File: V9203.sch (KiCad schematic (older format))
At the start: 62 parts, among them J1 RJ45, J4 Screw_Terminal_1x04, J6 CONN_01X06, J7 GS3, J8 GS3, U1 V9203, Y1 Crystal_GND24

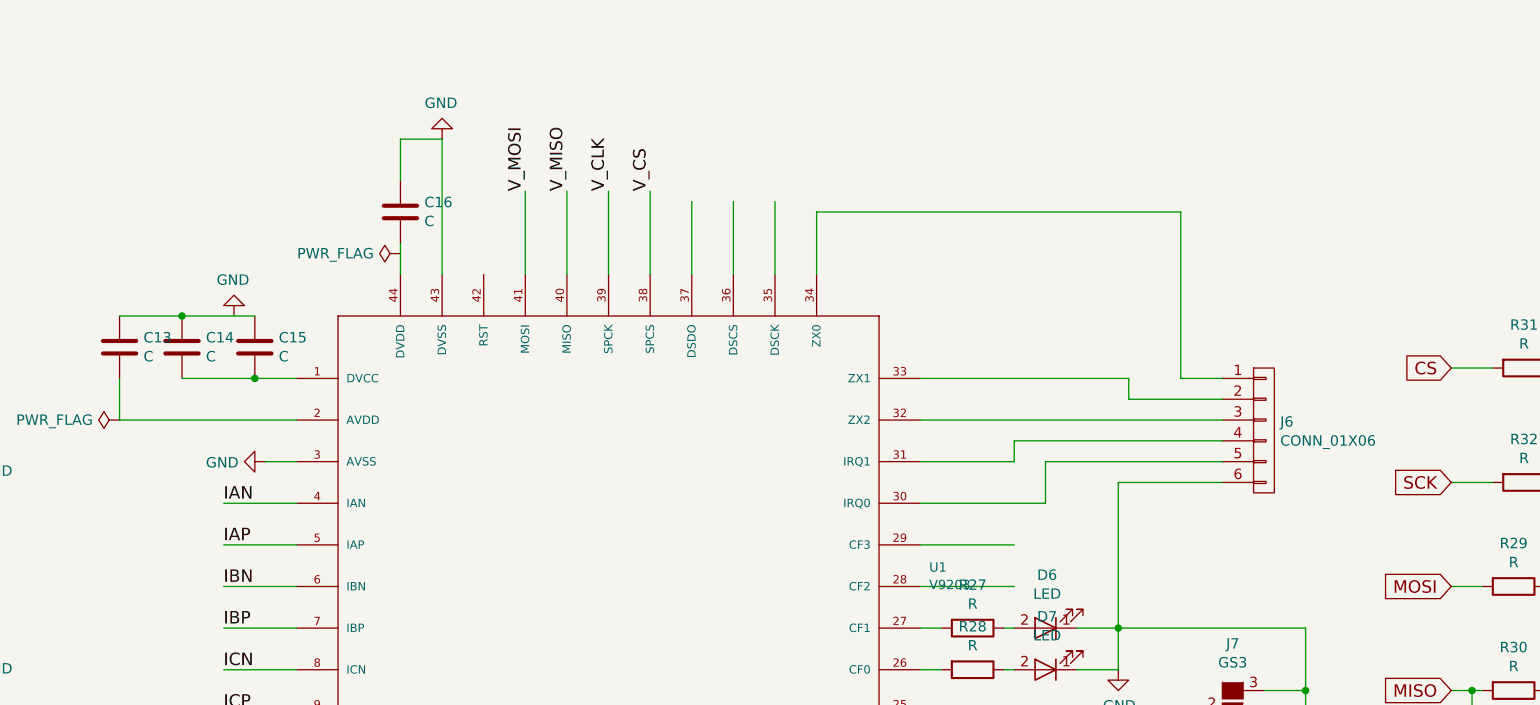
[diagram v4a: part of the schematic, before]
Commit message: Added more signals to JST connector including DMA
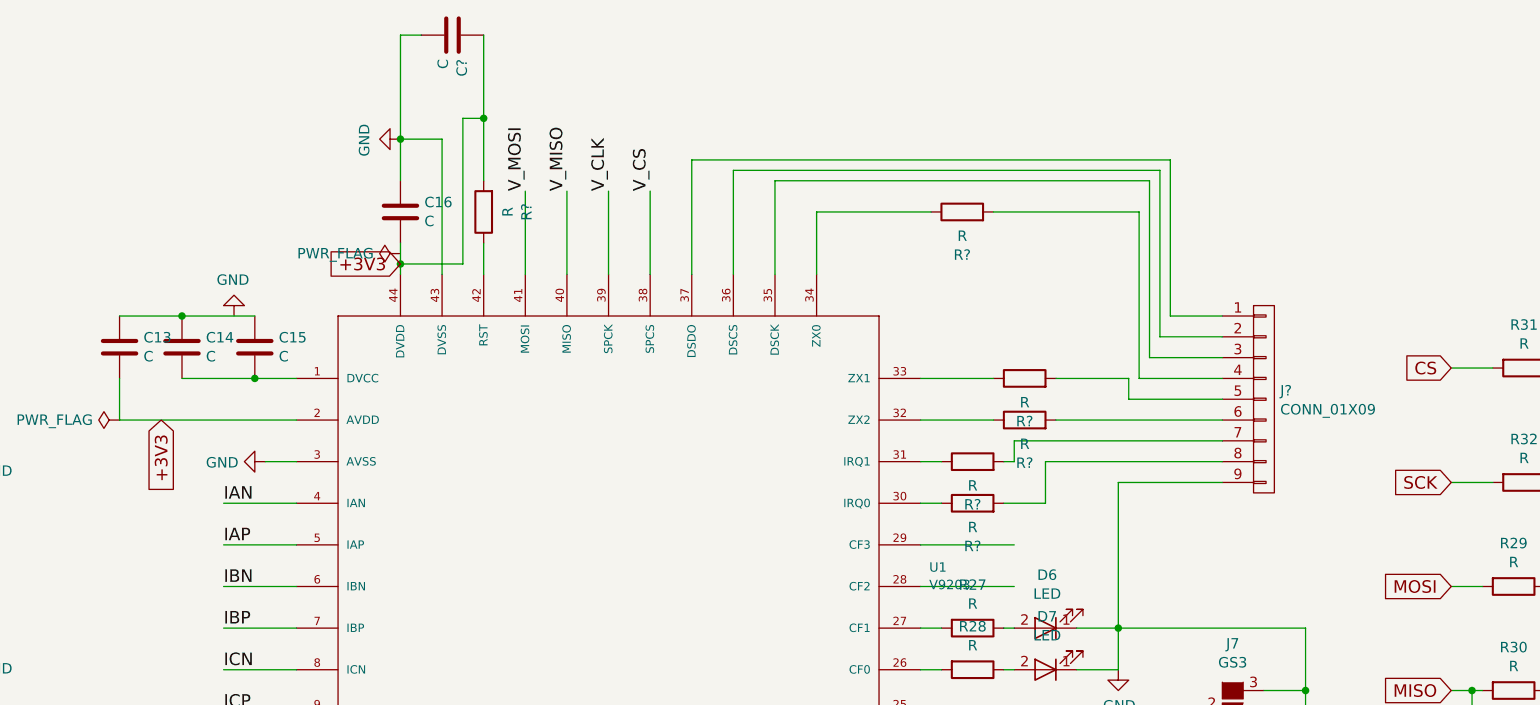
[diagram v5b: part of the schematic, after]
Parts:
- removed J6: CONN_01X06, Connectors_JST:JST_PH_B6B-PH-SM4-TB_06x2.00mm_Straight, symbol CONN_01X06
- added C?: C, Capacitors_SMD:C_0402, symbol C
- added J?: CONN_01X09, symbol CONN_01X09
- added R? (x6): R, Resistors_SMD:R_0402, symbol R
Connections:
- wire segments 167 -> 187

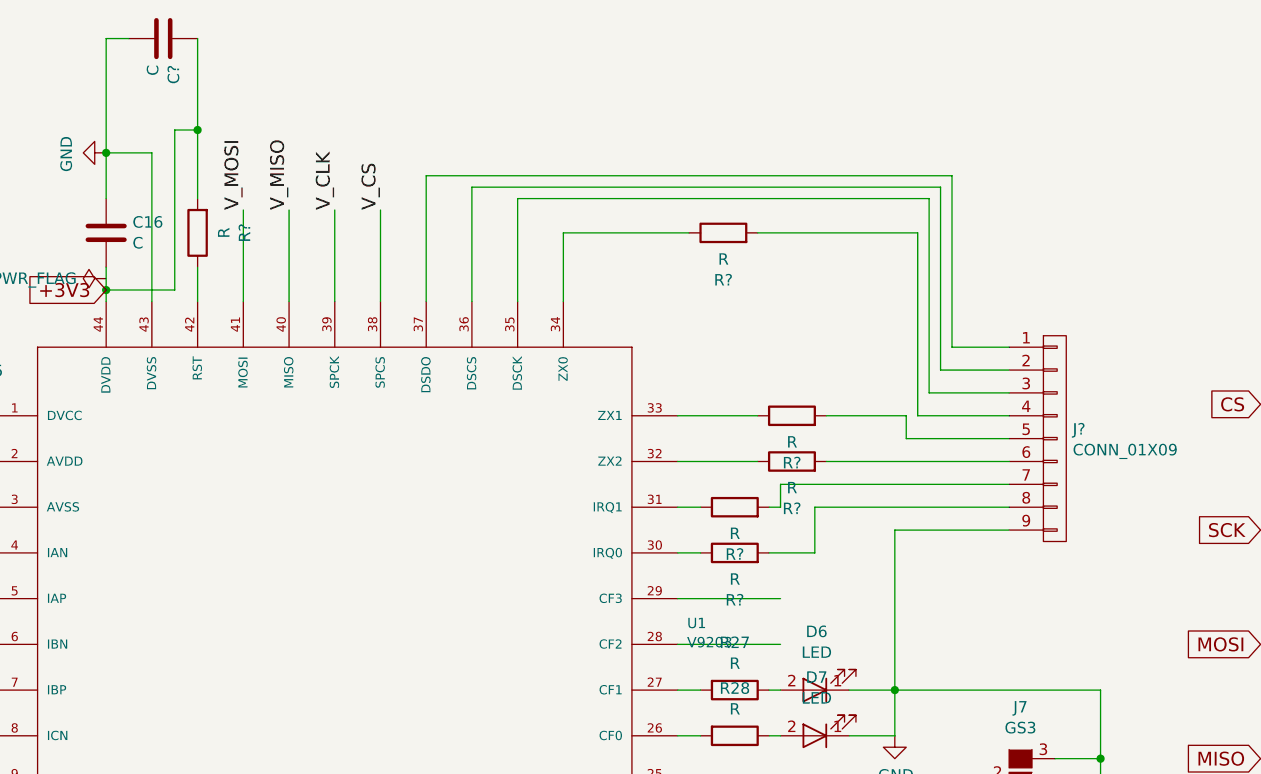
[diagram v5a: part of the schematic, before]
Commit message: Added more signals to JST connector including DMA
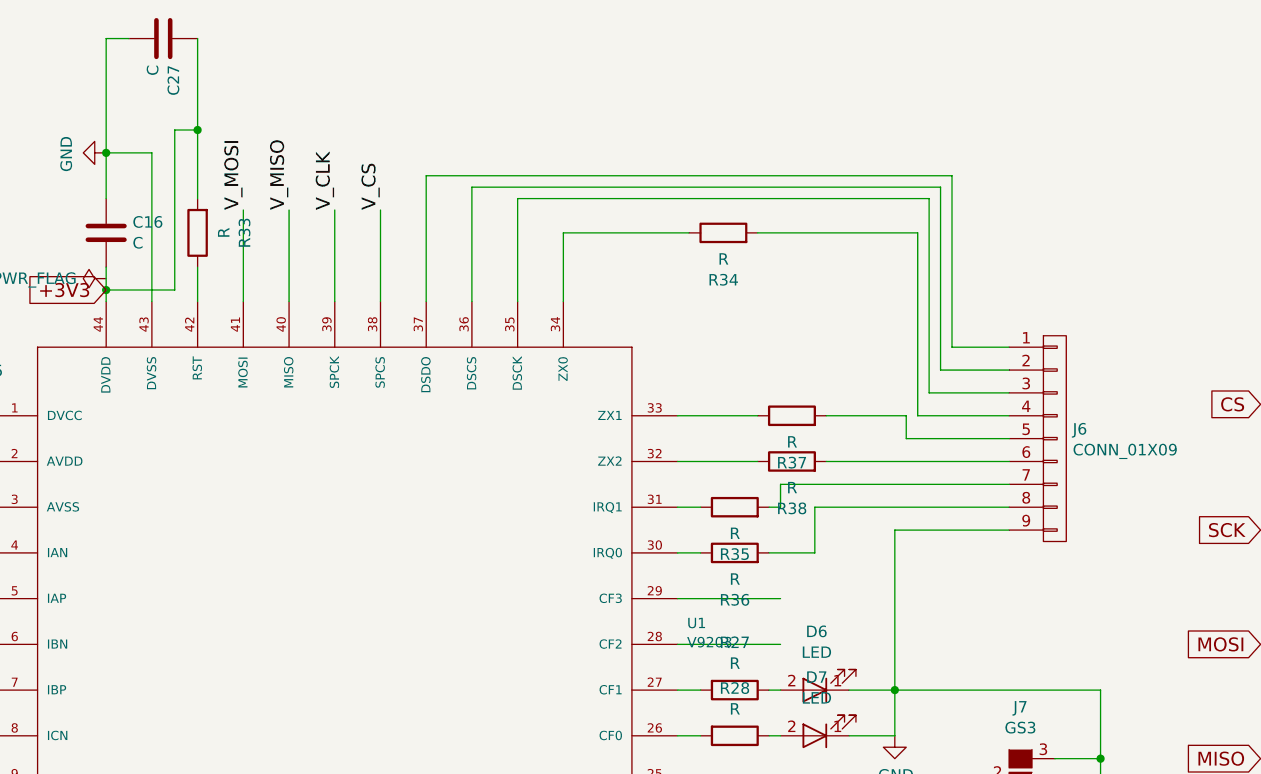
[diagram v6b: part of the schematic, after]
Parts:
- J6: renamed from J?; footprint (none) -> Connectors_JST:JST_SH_SM09B-SRSS-TB_09x1.00mm_Angled
- gave numbers to parts that had none: 7
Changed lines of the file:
@@
 +3V3
 $Comp
-L R R?
+L R R33
 U 1 1 5900142F
 P 5100 1700
-F 0 "R?" V 4893 1700 50  0000 C CNN
+F 0 "R33" V 4893 1700 50  0000 C CNN
 F 1 "R" V 4984 1700 50  0000 C CNN
 F 2 "Resistors_SMD:R_0402" V 2480 -450 50  0001 C CNN
@@
 $EndComp
 $Comp
-L C C?
+L C C27
 U 1 1 590019CE
 P 4950 850
-F 0 "C?" H 4835 804 50  0000 R CNN
+F 0 "C27" H 4835 804 50  0000 R CNN
 F 1 "C" H 4835 895 50  0000 R CNN
 F 2 "Capacitors_SMD:C_0402" H 3388 -2250 50  0001 C CNN
@@
 $EndComp
 $Comp
-L R R?
+L R R37
 U 1 1 590033EF
 P 7700 2500
-F 0 "R?" V 7493 2500 50  0000 C CNN
+F 0 "R37" V 7493 2500 50  0000 C CNN
 F 1 "R" V 7584 2500 50  0000 C CNN
 F 2 "Resistors_SMD:R_0402" V 5080 350 50  0001 C CNN
@@
 $EndComp
 $Comp
-L R R?
+L R R38
 U 1 1 59003D0A
 P 7700 2700
-F 0 "R?" V 7493 2700 50  0000 C CNN
+F 0 "R38" V 7493 2700 50  0000 C CNN
 F 1 "R" V 7584 2700 50  0000 C CNN
 F 2 "Resistors_SMD:R_0402" V 5080 550 50  0001 C CNN
@@
 $EndComp
 $Comp
-L R R?
+L R R35
 U 1 1 59003DA0
 P 7450 2900
-F 0 "R?" V 7243 2900 50  0000 C CNN
+F 0 "R35" V 7243 2900 50  0000 C CNN
 F 1 "R" V 7334 2900 50  0000 C CNN
 F 2 "Resistors_SMD:R_0402" V 4830 750 50  0001 C CNN
@@
 $EndComp
 $Comp
-L R R?
+L R R36
 U 1 1 59003E4E
 P 7450 3100
-F 0 "R?" V 7243 3100 50  0000 C CNN
+F 0 "R36" V 7243 3100 50  0000 C CNN
 F 1 "R" V 7334 3100 50  0000 C CNN
 F 2 "Resistors_SMD:R_0402" V 4830 950 50  0001 C CNN
@@
 	7850 2700 8650 2700
 $Comp
-L R R?
+L R R34
 U 1 1 59005ED9
 P 7400 1700
-F 0 "R?" V 7193 1700 50  0000 C CNN
+F 0 "R34" V 7193 1700 50  0000 C CNN
 F 1 "R" V 7284 1700 50  0000 C CNN
 F 2 "Resistors_SMD:R_0402" V 4780 -450 50  0001 C CNN
@@
 	8250 1700 7550 1700
 $Comp
-L CONN_01X09 J?
+L CONN_01X09 J6
 U 1 1 590073EE
 P 8850 2600
-F 0 "J?" H 8928 2641 50  0000 L CNN
+F 0 "J6" H 8928 2641 50  0000 L CNN
 F 1 "CONN_01X09" H 8928 2550 50  0000 L CNN
-F 2 "" H 0   500 50  0001 C CNN
+F 2 "Connectors_JST:JST_SH_SM09B-SRSS-TB_09x1.00mm_Angled" H 0   500 50  0001 C CNN
 F 3 "" H 0   500 50  0001 C CNN
 	1    8850 2600

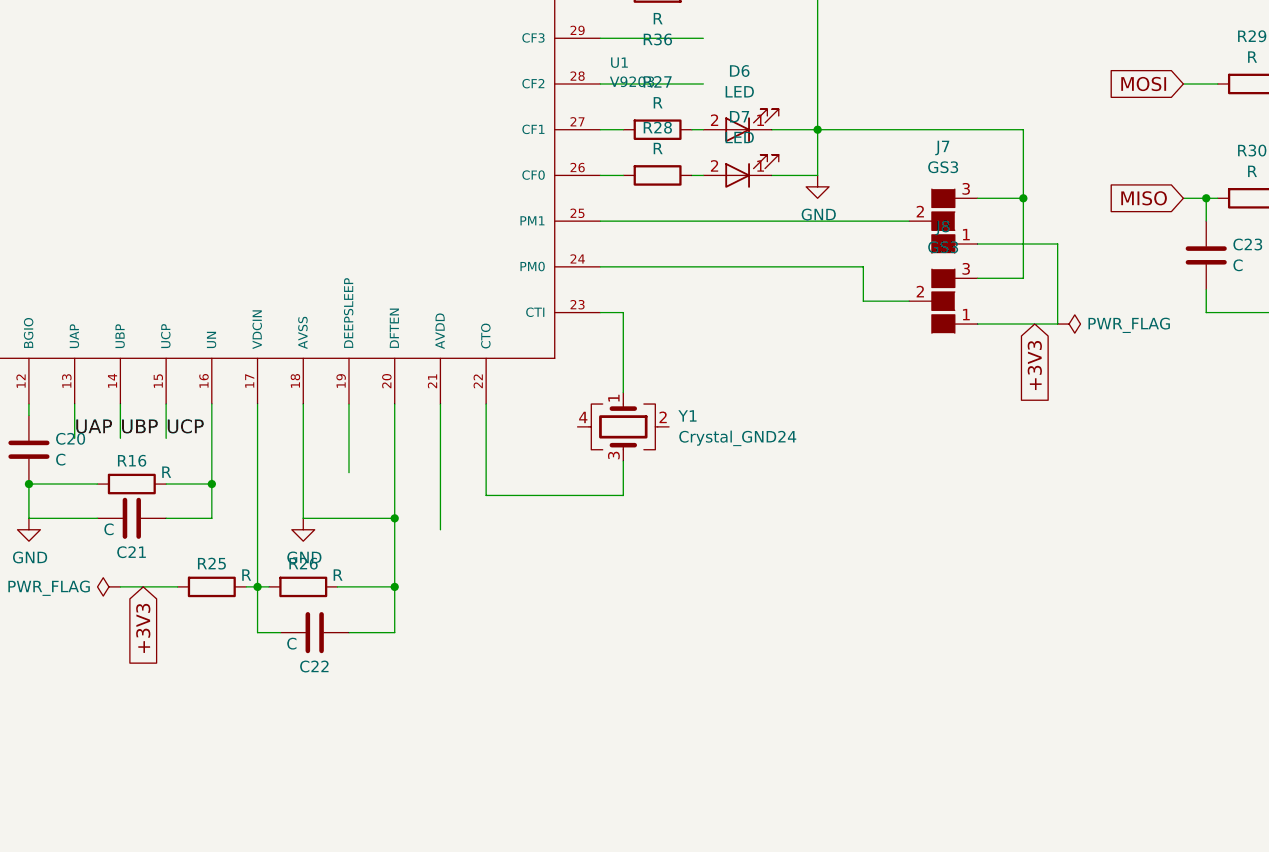
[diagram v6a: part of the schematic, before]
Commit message: Added PM0,1 and Deepsleep circuits
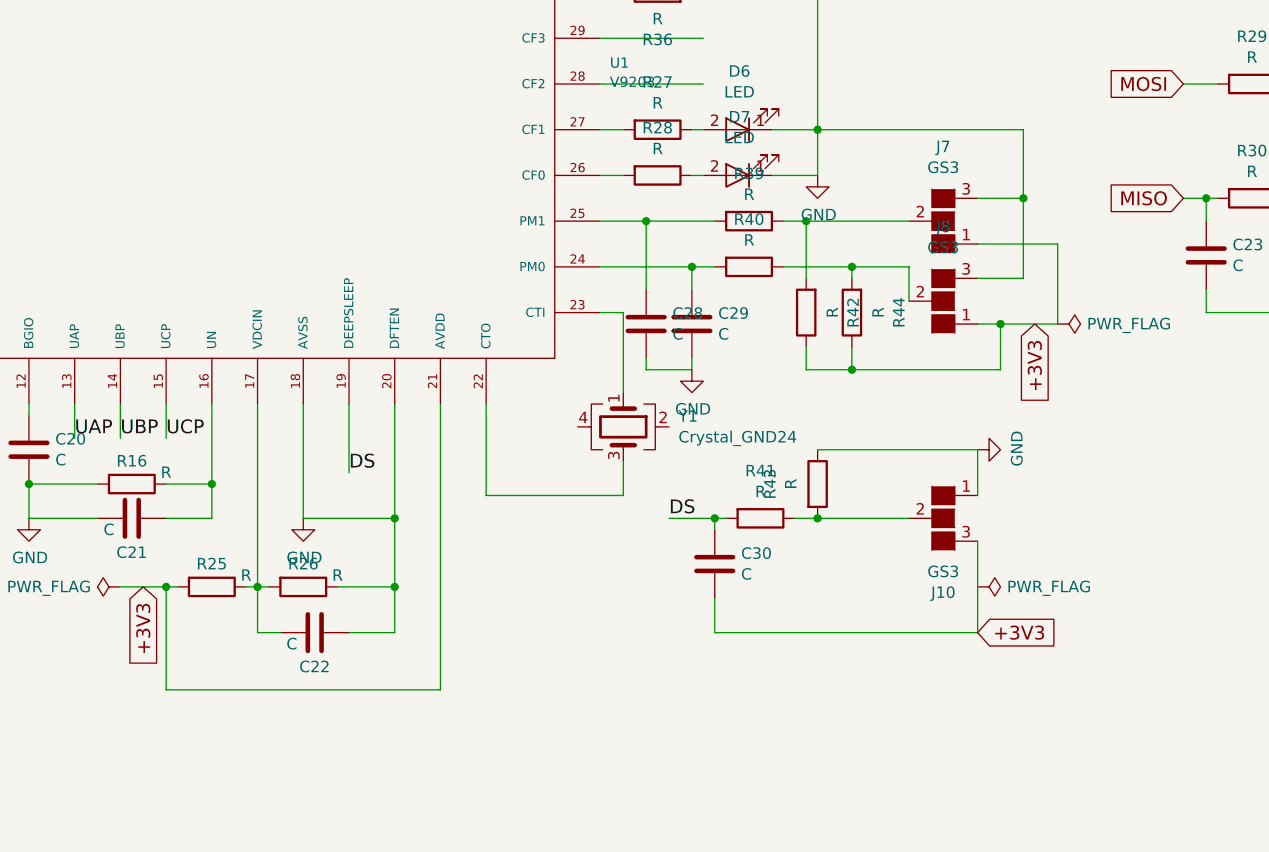
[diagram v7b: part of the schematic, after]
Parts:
- added C28, C29, C30: C, Capacitors_SMD:C_0402, symbol C
- added J10: GS3, Connect:GS3, symbol GS3
- added R39, R40, R41, R42, R43, R44: R, Resistors_SMD:R_0402, symbol R
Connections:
- net +3V3: now also U1.21 (AVDD), C30.2, J10.3 (G3), R42.1, R44.1
- net GND: now also C28.2, C29.2, J10.1 (G1), R43.1
- net DS: now reaches U1.19 (DEEPSLEEP)
- net DS: now also C30.1, R41.2
- net at U1.24 (PM0): now also C29.1, R40.2; no longer J8.2 (G2)
- net at U1.25 (PM1): now also C28.1, R39.2; no longer J7.2 (G2)
- new net: J7.2 (G2), R39.1, R42.2
- new net: J8.2 (G2), R40.1, R44.2
- new net: J10.2 (G2), R41.1, R43.2
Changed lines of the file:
@@
 LIBS:logo
 LIBS:mechanical
+LIBS:whatnick
 LIBS:V9203_Devkit-cache
 EELAYER 26 0
@@
 	7200 3500 7650 3500
 Wire Wire Line
-	7200 4100 8550 4100
-Wire Wire Line
-	7200 4300 8350 4300
-Wire Wire Line
 	5700 4900 5700 5900
 Wire Wire Line
 	5900 4900 5900 5400
 Wire Wire Line
-	6500 4900 6500 5450
+	6500 4900 6500 6150
 Wire Wire Line
 	6300 4900 6300 5900
@@
 Connection ~ 2050 3900
 Connection ~ 1000 3900
-Wire Wire Line
-	8350 4300 8350 4450
-Wire Wire Line
-	8350 4450 8550 4450
 Wire Wire Line
 	8850 4200 9200 4200
@@
 	1    0    0    -1
 $EndComp
+Wire Wire Line
+	6500 6150 5300 6150
+Wire Wire Line
+	5300 6150 5300 5700
+Connection ~ 5300 5700
+$Comp
+L R R39
+U 1 1 59059E80
+P 7850 4100
+F 0 "R39" V 7643 4100 50  0000 C CNN
+F 1 "R" V 7734 4100 50  0000 C CNN
+F 2 "Resistors_SMD:R_0402" V 5230 1950 50  0001 C CNN
+F 3 "" H 5300 1950 50  0001 C CNN
+	1    7850 4100
+	0    1    1    0
+$EndComp
+$Comp
+L R R40
+U 1 1 59059F4E
+P 7850 4300
+F 0 "R40" V 7643 4300 50  0000 C CNN
+F 1 "R" V 7734 4300 50  0000 C CNN
+F 2 "Resistors_SMD:R_0402" V 5230 2150 50  0001 C CNN
+F 3 "" H 5300 2150 50  0001 C CNN
+	1    7850 4300
+	0    1    1    0
+$EndComp
+$Comp
+L R R42
+U 1 1 5905A02E
+P 8100 4500
+F 0 "R42" V 7893 4500 50  0000 C CNN
+F 1 "R" V 7984 4500 50  0000 C CNN
+F 2 "Resistors_SMD:R_0402" V 5480 2350 50  0001 C CNN
+F 3 "" H 5550 2350 50  0001 C CNN
+	1    8100 4500
+	-1   0    0    1
+$EndComp
+$Comp
+L R R44
+U 1 1 5905A13A
+P 8300 4500
+F 0 "R44" V 8093 4500 50  0000 C CNN
+F 1 "R" V 8184 4500 50  0000 C CNN
+F 2 "Resistors_SMD:R_0402" V 5680 2350 50  0001 C CNN
+F 3 "" H 5750 2350 50  0001 C CNN
+	1    8300 4500
+	-1   0    0    1
+$EndComp
+$Comp
+L C C28
+U 1 1 5905A1EE
+P 7400 4550
+F 0 "C28" H 7515 4596 50  0000 L CNN
+F 1 "C" H 7515 4505 50  0000 L CNN
+F 2 "Capacitors_SMD:C_0402" H 5838 1450 50  0001 C CNN
+F 3 "" H 5800 1600 50  0001 C CNN
+	1    7400 4550
+	1    0    0    -1
+$EndComp
+$Comp
+L C C29
+U 1 1 5905A4AC
+P 7600 4550
+F 0 "C29" H 7715 4596 50  0000 L CNN
+F 1 "C" H 7715 4505 50  0000 L CNN
+F 2 "Capacitors_SMD:C_0402" H 6038 1450 50  0001 C CNN
+F 3 "" H 6000 1600 50  0001 C CNN
+	1    7600 4550
+	1    0    0    -1
+$EndComp
+Wire Wire Line
+	7200 4100 7700 4100
+Wire Wire Line
+	8000 4100 8550 4100
+Wire Wire Line
+	7200 4300 7700 4300
+Wire Wire Line
+	8000 4300 8550 4300
+Wire Wire Line
+	8550 4300 8550 4450
+Wire Wire Line
+	8300 4350 8300 4300
+Connection ~ 8300 4300
+Wire Wire Line
+	8100 4350 8100 4100
+Connection ~ 8100 4100
+Wire Wire Line
+	8100 4650 8100 4750
+Wire Wire Line
+	8100 4750 8950 4750
+Wire Wire Line
+	8300 4750 8300 4650
+Wire Wire Line
+	8950 4750 8950 4550
+Connection ~ 8950 4550
+Connection ~ 8300 4750
+Wire Wire Line
+	7400 4400 7400 4100
+Connection ~ 7400 4100
+Wire Wire Line
+	7600 4400 7600 4300
+Connection ~ 7600 4300
+Wire Wire Line
+	7400 4700 7400 4750
+Wire Wire Line
+	7400 4750 7600 4750
+Wire Wire Line
+	7600 4750 7600 4700
+$Comp
+L GND #PWR019
+U 1 1 5905C1C0
+P 7600 4750
+F 0 "#PWR019" H 2800 2500 50  0001 C CNN
+F 1 "GND" H 7605 4577 50  0000 C CNN
+F 2 "" H 2800 2750 50  0001 C CNN
+F 3 "" H 2800 2750 50  0001 C CNN
+	1    7600 4750
+	1    0    0    -1
+$EndComp
+Text Label 6100 5200 0    60   ~ 0
+DS
+$Comp
+L C C30
+U 1 1 5905E737
+P 7700 5600
+F 0 "C30" H 7815 5646 50  0000 L CNN
+F 1 "C" H 7815 5555 50  0000 L CNN
+F 2 "Capacitors_SMD:C_0402" H 6138 2500 50  0001 C CNN
+F 3 "" H 6100 2650 50  0001 C CNN
+	1    7700 5600
+	1    0    0    -1
+$EndComp
+$Comp
+L R R41
+U 1 1 5905E7FB
+P 7900 5400
+F 0 "R41" V 7693 5400 50  0000 C CNN
+F 1 "R" V 7784 5400 50  0000 C CNN
+F 2 "Resistors_SMD:R_0402" V 5280 3250 50  0001 C CNN
+F 3 "" H 5350 3250 50  0001 C CNN
+	1    7900 5400
+	0    1    1    0
+$EndComp
+$Comp
+L R R43
+U 1 1 5905E8C5
+P 8150 5250
+F 0 "R43" V 7943 5250 50  0000 C CNN
+F 1 "R" V 8034 5250 50  0000 C CNN
+F 2 "Resistors_SMD:R_0402" V 5530 3100 50  0001 C CNN
+F 3 "" H 5600 3100 50  0001 C CNN
+	1    8150 5250
+	1    0    0    -1
+$EndComp
+$Comp
+L GS3 J10
+U 1 1 5905E99D
+P 8700 5400
+F 0 "J10" H 8700 5075 50  0000 C CNN
+F 1 "GS3" H 8700 5166 50  0000 C CNN
+F 2 "Connect:GS3" V -762 126 50  0001 C CNN
+F 3 "" H -850 200 50  0001 C CNN
+	1    8700 5400
+	-1   0    0    -1
+$EndComp
+Wire Wire Line
+	7500 5400 7750 5400
+Wire Wire Line
+	7700 5450 7700 5400
+Connection ~ 7700 5400
+Wire Wire Line
+	7700 5750 7700 5900
+Wire Wire Line
+	7700 5900 8850 5900
+Wire Wire Line
+	8050 5400 8550 5400
+Connection ~ 8150 5400
+Wire Wire Line
+	8850 5900 8850 5500
+Wire Wire Line
+	8150 5100 8850 5100
+Wire Wire Line
+	8850 5100 8850 5300
+Text Label 7500 5400 0    60   ~ 0
+DS
+Text GLabel 8850 5900 2    60   Input ~ 0
++3V3
+$Comp
+L PWR_FLAG #FLG020
+U 1 1 5905FDEF
+P 8850 5700
+F 0 "#FLG020" H 4000 3875 50  0001 C CNN
+F 1 "PWR_FLAG" V 8850 5828 50  0000 L CNN
+F 2 "" H 4000 3800 50  0001 C CNN
+F 3 "" H 4000 3800 50  0001 C CNN
+	1    8850 5700
+	0    1    1    0
+$EndComp
+$Comp
+L GND #PWR021
+U 1 1 59060110
+P 8850 5100
+F 0 "#PWR021" H 4050 2850 50  0001 C CNN
+F 1 "GND" H 8855 4927 50  0000 C CNN
+F 2 "" H 4050 3100 50  0001 C CNN
+F 3 "" H 4050 3100 50  0001 C CNN
+	1    8850 5100
+	0    -1   -1   0
+$EndComp
 $EndSCHEMATC
